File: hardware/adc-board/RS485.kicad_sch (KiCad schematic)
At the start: 4 parts, among them J6 54601-908WPLF, U14 ISL83490

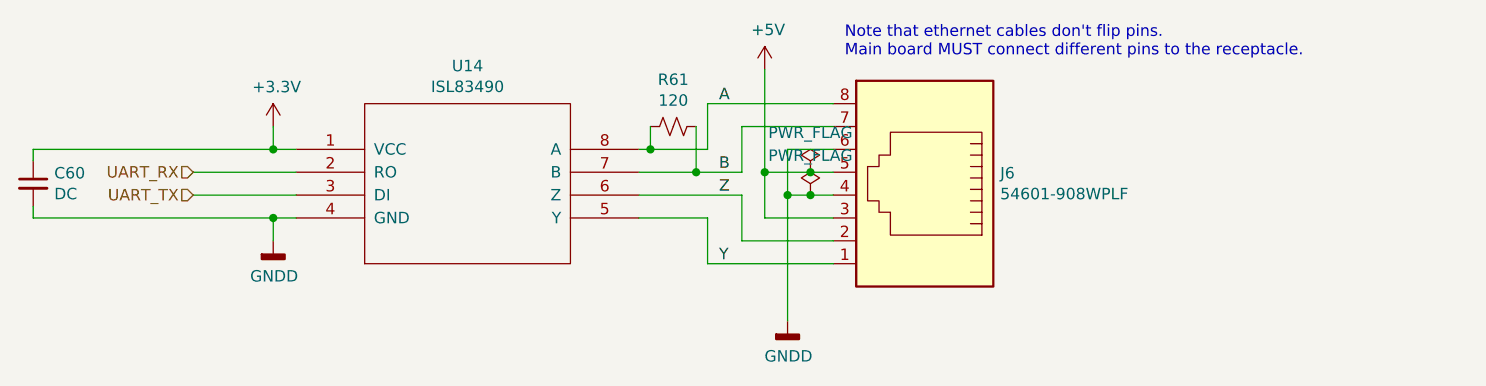
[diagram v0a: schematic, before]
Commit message: Unified ground nets in schematic and layout.
* Rearranged the layers that pours are on.
* Added the keep-out zone separating analog and
  digital areas from each other.
* Tightened up placement of decoupling capacitors.
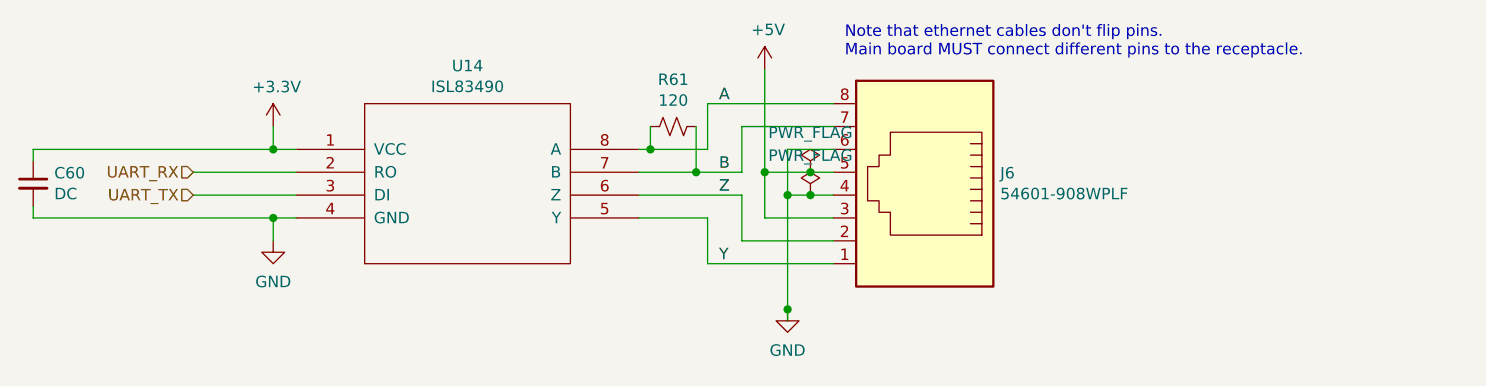
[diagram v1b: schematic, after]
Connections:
- net GNDD renamed GND
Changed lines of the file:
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@@
   (junction (at 175.26 96.52) (diameter 0) (color 0 0 0 0)
   )
+  (junction (at 175.26 109.22) (diameter 0) (color 0 0 0 0)
+  )
   (junction (at 177.8 93.98) (diameter 0) (color 0 0 0 0)
   )
@@
     (stroke (width 0) (type default) (color 0 0 0 0))
   )
-  (wire (pts (xy 175.26 96.52) (xy 175.26 110.49))
+  (wire (pts (xy 175.26 96.52) (xy 175.26 109.22))
     (stroke (width 0) (type default) (color 0 0 0 0))
   )
@@
   )
   (wire (pts (xy 177.8 96.52) (xy 175.26 96.52))
+    (stroke (width 0) (type default) (color 0 0 0 0))
+  )
+  (wire (pts (xy 175.26 109.22) (xy 175.26 110.49))
     (stroke (width 0) (type default) (color 0 0 0 0))
   )
@@
     )
     (property "Datasheet" "" (id 3) (at 118.11 88.9 0)
-      (effects (font (size 1.27 1.27)) hide)
-    )
-    (pin "1")
-  )
-  (symbol (lib_id "power:GNDD") (at 118.11 101.6 0) (unit 1)
-    (in_bom yes) (on_board yes)
-    (property "Reference" "#PWR0118" (id 0) (at 118.11 107.95 0)
-      (effects (font (size 1.27 1.27)) hide)
-    )
-    (property "Value" "GNDD" (id 1) (at 118.2116 105.537 0))
-    (property "Footprint" "" (id 2) (at 118.11 101.6 0)
-      (effects (font (size 1.27 1.27)) hide)
-    )
-    (property "Datasheet" "" (id 3) (at 118.11 101.6 0)
       (effects (font (size 1.27 1.27)) hide)
     )
@@
     (pin "8")
   )
-  (symbol (lib_id "power:GNDD") (at 175.26 110.49 0) (unit 1)
-    (in_bom yes) (on_board yes)
-    (property "Reference" "#PWR0134" (id 0) (at 175.26 116.84 0)
-      (effects (font (size 1.27 1.27)) hide)
-    )
-    (property "Value" "GNDD" (id 1) (at 175.3616 114.427 0))
-    (property "Footprint" "" (id 2) (at 175.26 110.49 0)
-      (effects (font (size 1.27 1.27)) hide)
-    )
-    (property "Datasheet" "" (id 3) (at 175.26 110.49 0)
-      (effects (font (size 1.27 1.27)) hide)
-    )
-    (pin "1")
-  )
   (symbol (lib_id "ISL83490:ISL83490") (at 139.7 95.25 0) (unit 1)
     (in_bom yes) (on_board yes)
@@
     (pin "2")
   )
+  (symbol (lib_id "power:GND") (at 175.26 109.22 0) (unit 1)
+    (in_bom yes) (on_board yes) (fields_autoplaced)
+    (property "Reference" "#PWR0141" (id 0) (at 175.26 115.57 0)
+      (effects (font (size 1.27 1.27)) hide)
+    )
+    (property "Value" "GND" (id 1) (at 175.26 113.7825 0))
+    (property "Footprint" "" (id 2) (at 175.26 109.22 0)
+      (effects (font (size 1.27 1.27)) hide)
+    )
+    (property "Datasheet" "" (id 3) (at 175.26 109.22 0)
+      (effects (font (size 1.27 1.27)) hide)
+    )
+    (pin "1")
+  )
+  (symbol (lib_id "power:GND") (at 118.11 101.6 0) (unit 1)
+    (in_bom yes) (on_board yes) (fields_autoplaced)
+    (property "Reference" "#PWR0144" (id 0) (at 118.11 107.95 0)
+      (effects (font (size 1.27 1.27)) hide)
+    )
+    (property "Value" "GND" (id 1) (at 118.11 106.1625 0))
+    (property "Footprint" "" (id 2) (at 118.11 101.6 0)
+      (effects (font (size 1.27 1.27)) hide)
+    )
+    (property "Datasheet" "" (id 3) (at 118.11 101.6 0)
+      (effects (font (size 1.27 1.27)) hide)
+    )
+    (pin "1")
+  )
 )

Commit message: More ADC board rev 3 changes, per issue #47
* 4.5V regulator for phototransistors
* new 3.3V regulator for analog section
* new 2.0V precision voltage reference
* Analog voltages and their distribution rearranged
* Tidied up traces on the left hand side, everything is nice and curvy now
* Adjusted USB ESD protection to be optional and/or support other parts
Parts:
- C60: footprint Capacitors_SMD:C_0805 -> Capacitor_SMD:C_0805_2012Metric
- R61: footprint Resistors_SMD:R_0805 -> Resistor_SMD:R_0805_2012Metric
- U14: footprint SMD_Packages:SOIC-8-N -> Package_SO:SOP-8_3.9x4.9mm_P1.27mm
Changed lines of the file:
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@@
     (property "Reference" "U14" (id 0) (at 139.7 82.169 0))
     (property "Value" "ISL83490" (id 1) (at 139.7 84.4804 0))
-    (property "Footprint" "SMD_Packages:SOIC-8-N" (id 2) (at 139.7 95.25 0)
+    (property "Footprint" "Package_SO:SOP-8_3.9x4.9mm_P1.27mm" (id 2) (at 139.7 95.25 0)
       (effects (font (size 1.27 1.27)) hide)
     )
@@
     (property "Reference" "R61" (id 0) (at 162.56 83.693 90))
     (property "Value" "120" (id 1) (at 162.56 86.0044 90))
-    (property "Footprint" "Resistors_SMD:R_0805" (id 2) (at 162.56 88.9 0)
+    (property "Footprint" "Resistor_SMD:R_0805_2012Metric" (id 2) (at 162.56 88.9 0)
       (effects (font (size 1.27 1.27)) hide)
     )
@@
       (effects (font (size 1.27 1.27)) (justify left))
     )
-    (property "Footprint" "Capacitors_SMD:C_0805" (id 2) (at 91.44 95.25 0)
+    (property "Footprint" "Capacitor_SMD:C_0805_2012Metric" (id 2) (at 91.44 95.25 0)
       (effects (font (size 1.27 1.27)) hide)
     )
